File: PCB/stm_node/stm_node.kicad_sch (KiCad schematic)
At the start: 2 parts, among them U1 NRF24L01_Breakout

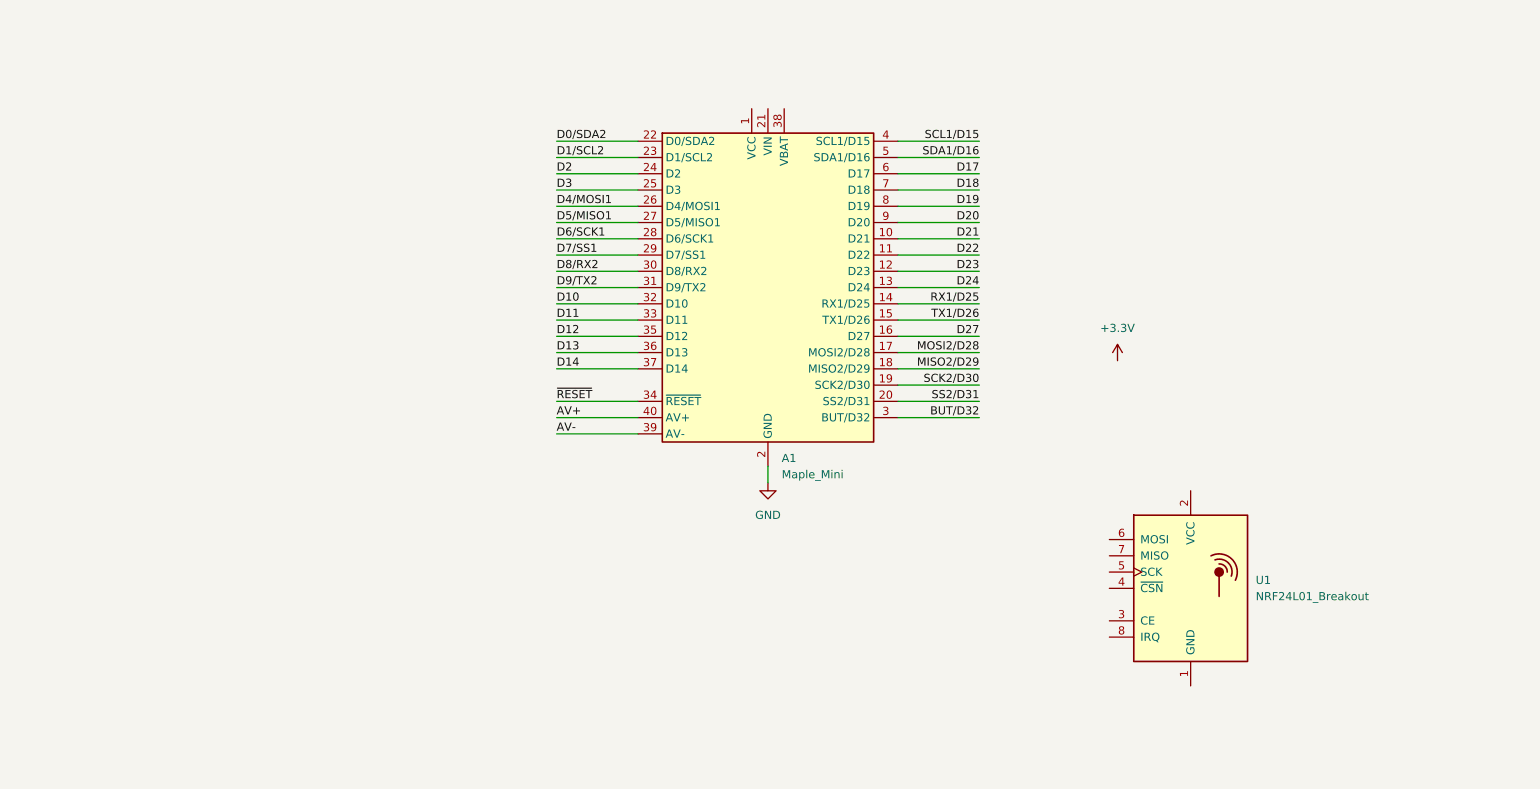
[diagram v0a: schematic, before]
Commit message: ML Model added and implemented on pico
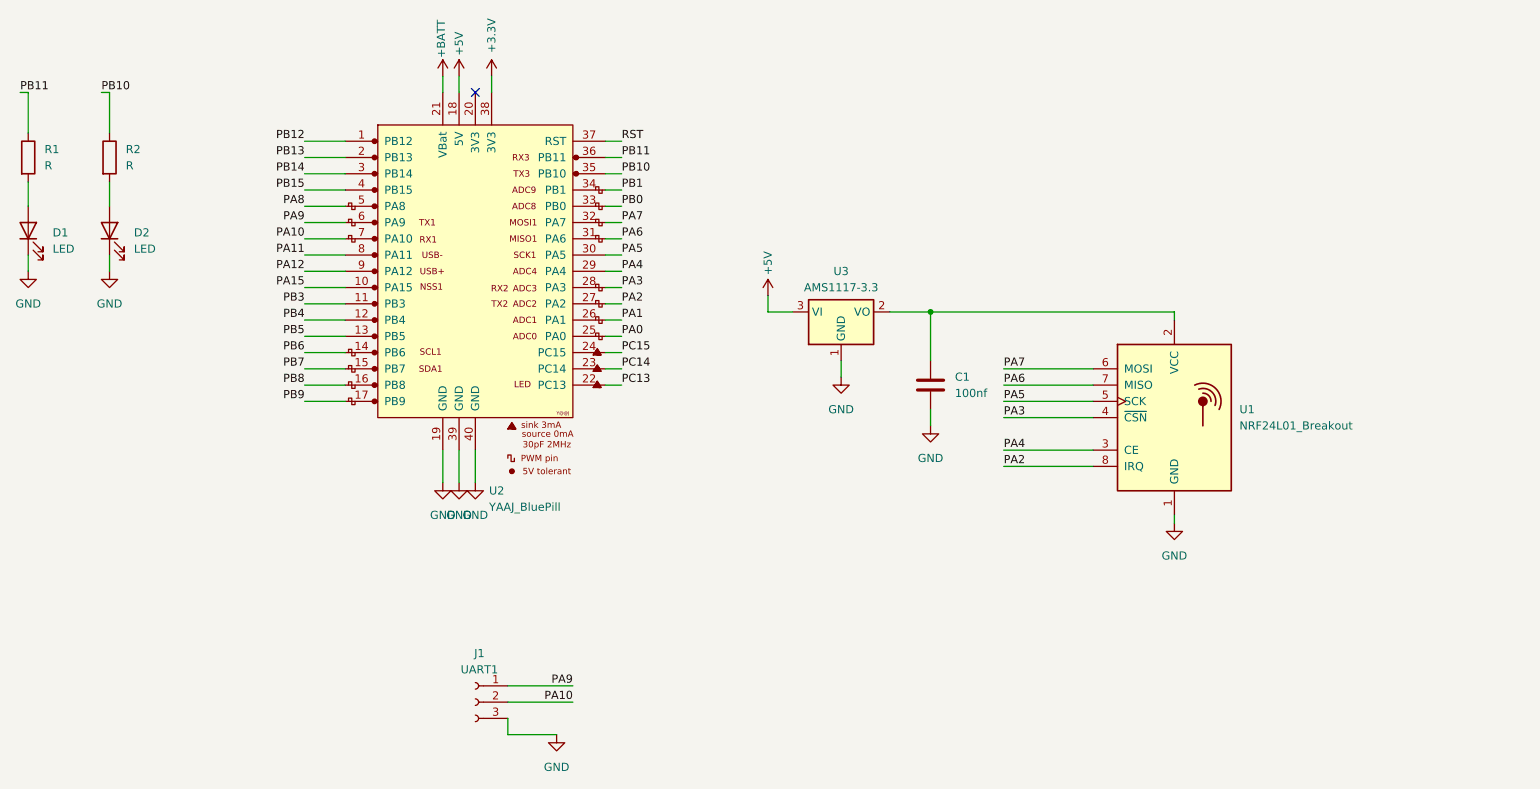
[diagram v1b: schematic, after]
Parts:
- removed A1: Maple_Mini, Module:Maple_Mini, symbol MCU_Module:Maple_Mini
- added C1: 100nf, Capacitor_Tantalum_SMD:CP_EIA-3528-12_Kemet-T_HandSolder, symbol Device:C
- added D1, D2: LED, LED_THT:LED_D5.0mm, symbol Device:LED
- added J1: UART1, Connector_JST:JST_XH_B3B-XH-A_1x03_P2.50mm_Vertical, symbol Connector:Conn_01x03_Socket
- added R1, R2: R, Resistor_THT:R_Axial_DIN0207_L6.3mm_D2.5mm_P10.16mm_Horizontal, symbol Device:R
- added U2: YAAJ_BluePill, footprints:YAAJ_BluePill_1, symbol YAAJ_BluePill:YAAJ_BluePill
- added U3: AMS1117-3.3, Package_TO_SOT_SMD:SOT-223-3_TabPin2, symbol Regulator_Linear:AMS1117-3.3
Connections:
- net +3.3V: now also U2.38 (3V3)
- net GND: now also U1.1 (GND), C1.2, D1.1 (K), D2.1 (K), J1.3 (Pin_3), U2.19 (GND), U2.39 (GND), U2.40 (GND), U3.1 (GND)
- net at U1.2 (VCC): now also C1.1, U3.2 (VO)
- net PA4: now reaches U1.3 (CE)
- net PA4: now also U2.29 (PA4)
- net PA3: now reaches U1.4 (~{CSN})
- net PA3: now also U2.28 (PA3)
- net PA5: now reaches U1.5 (SCK)
- net PA5: now also U2.30 (PA5)
- net PA7: now reaches U1.6 (MOSI)
- net PA7: now also U2.32 (PA7)
- net PA6: now reaches U1.7 (MISO)
- net PA6: now also U2.31 (PA6)
- net PA2: now reaches U1.8 (IRQ)
- net PA2: now also U2.27 (PA2)
- new net: D2.2 (A), R2.2
- new net: D1.2 (A), R1.2
- new net +5V: U2.18 (5V), U3.3 (VI)
- new net +BATT: U2.21 (VBat)
- new net PA0: U2.25 (PA0)
- new net PA1: U2.26 (PA1)
- new net PA10: J1.2 (Pin_2), U2.7 (PA10)
- new net PA11: U2.8 (PA11)
- new net PA12: U2.9 (PA12)
- new net PA15: U2.10 (PA15)
- new net PA8: U2.5 (PA8)
- new net PA9: J1.1 (Pin_1), U2.6 (PA9)
- new net PB0: U2.33 (PB0)
- new net PB1: U2.34 (PB1)
- new net PB10: R2.1, U2.35 (PB10)
- new net PB11: R1.1, U2.36 (PB11)
- new net PB12: U2.1 (PB12)
- new net PB13: U2.2 (PB13)
- new net PB14: U2.3 (PB14)
- new net PB15: U2.4 (PB15)
- new net PB3: U2.11 (PB3)
- new net PB4: U2.12 (PB4)
- new net PB5: U2.13 (PB5)
- new net PB6: U2.14 (PB6)
- new net PB7: U2.15 (PB7)
- new net PB8: U2.16 (PB8)
- new net PB9: U2.17 (PB9)
- new net PC13: U2.22 (PC13)
- new net PC14: U2.23 (PC14)
- new net PC15: U2.24 (PC15)
- new net RST: U2.37 (RST)
- no-connect marks 0 -> 1
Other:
- moved on the sheet: U1

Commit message: updated ML model using Edge impulse updated INMP441 pio code
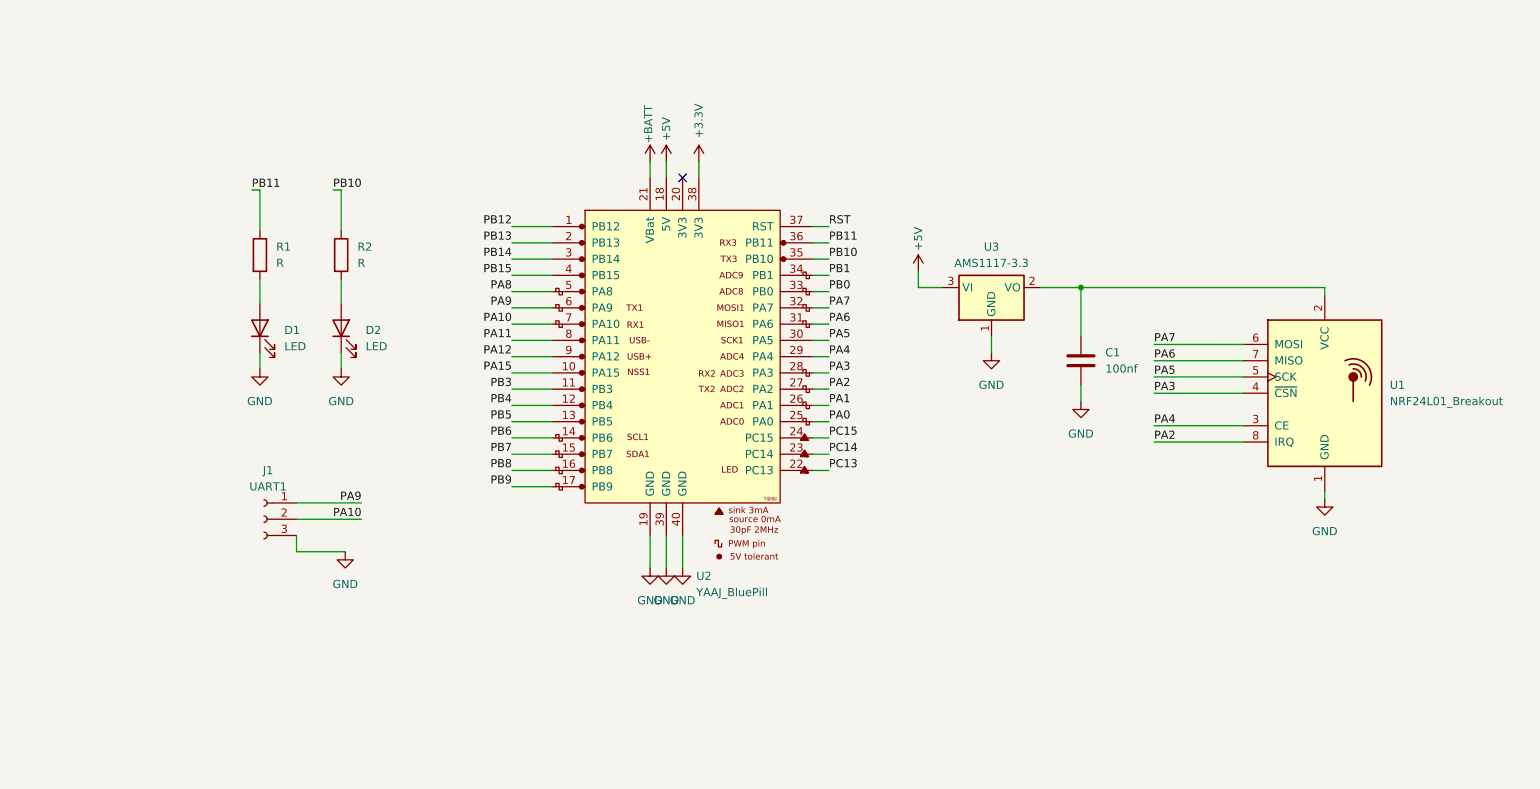
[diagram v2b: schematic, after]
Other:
- company: (none) -> RV College of Engineering 
- title: (none) -> IDP Project Central Node
- moved on the sheet: C1, D1, D2, J1, R1, R2, U1, U2, U3
